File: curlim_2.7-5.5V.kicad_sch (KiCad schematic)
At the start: 9 parts, among them J11 Conn_01x02, J12 Conn_01x04, U4 AP22653AW6-7, U5 INA199A1DCKR

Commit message: WIP v0.2.0 changes
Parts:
- added R81: 10k, Resistor_SMD:R_0603_1608Metric_Pad0.98x0.95mm_HandSolder, symbol Device:R_Small
- RV1: LCSC (none) -> C118942; THT_LCSC C118942 -> (none)
- renumbered J11 to J10, J12 to J11
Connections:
- net EN: now also R81.1
- net GND: now also J10.1 (Pin_1), R81.2; no longer J10.2 (Pin_2)
- net ILIM: now also J10.2 (Pin_2); no longer J10.1 (Pin_1)

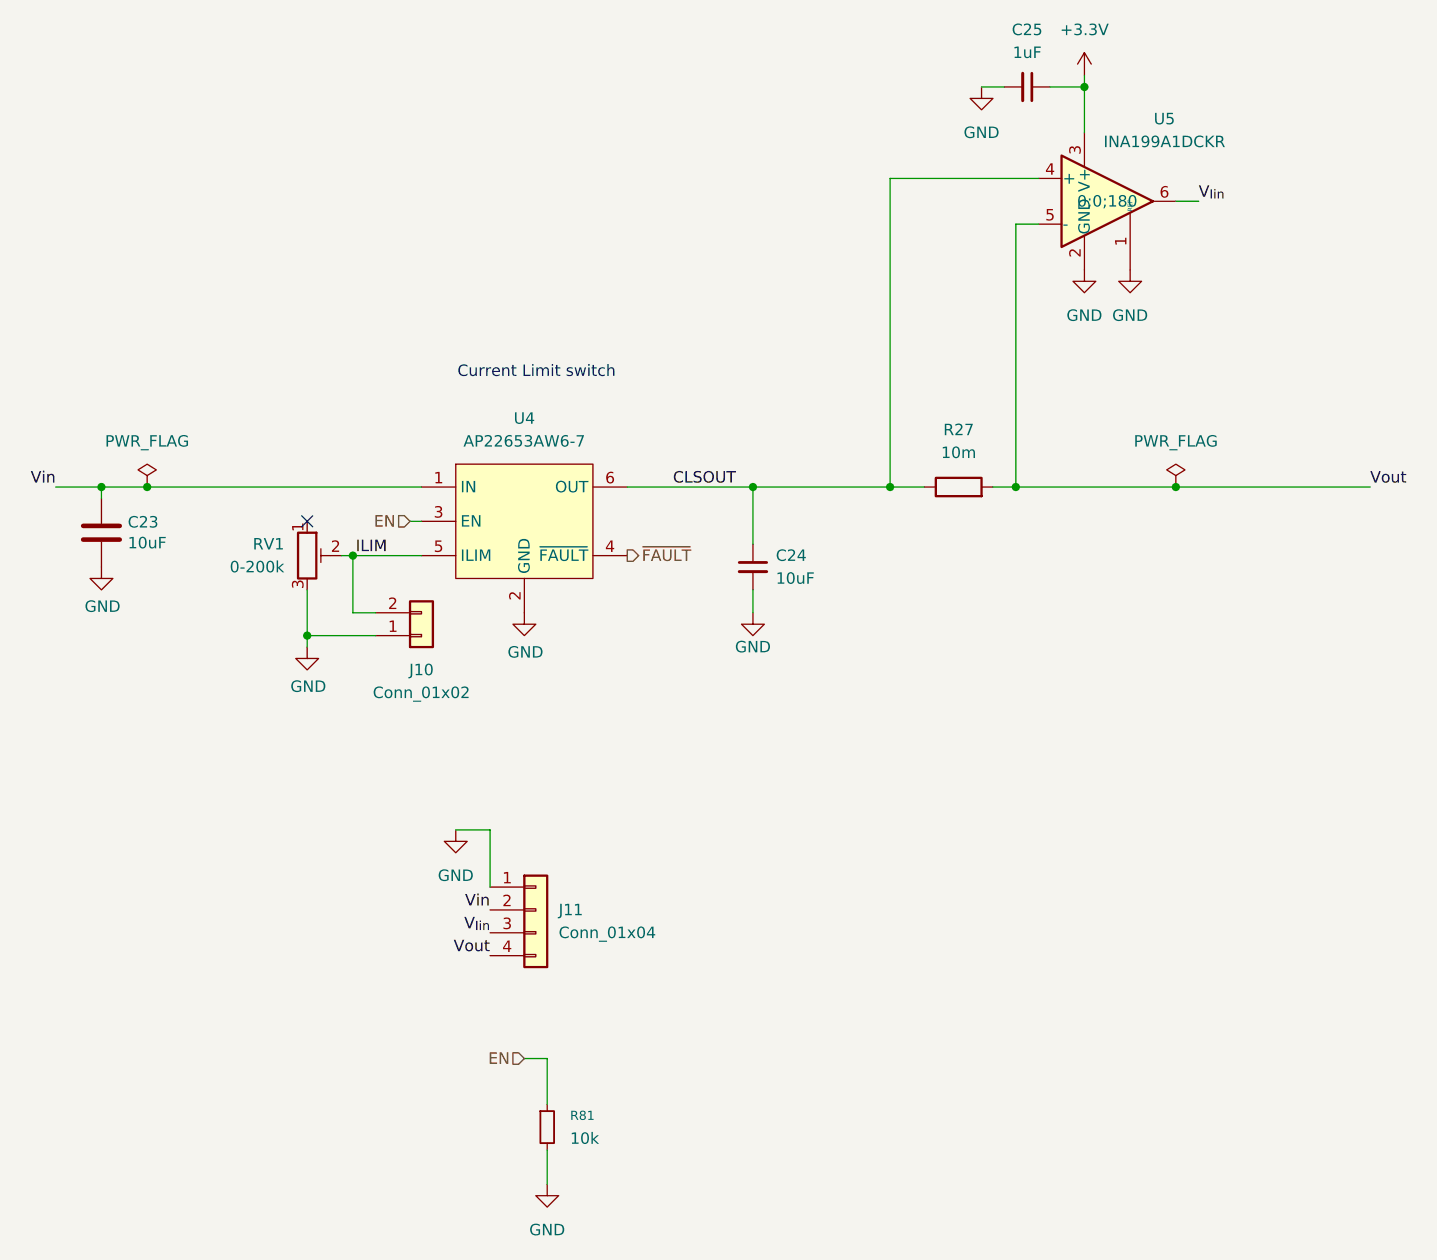
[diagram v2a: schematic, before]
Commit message: Assign part numbers and finish other 0.2.0 changes
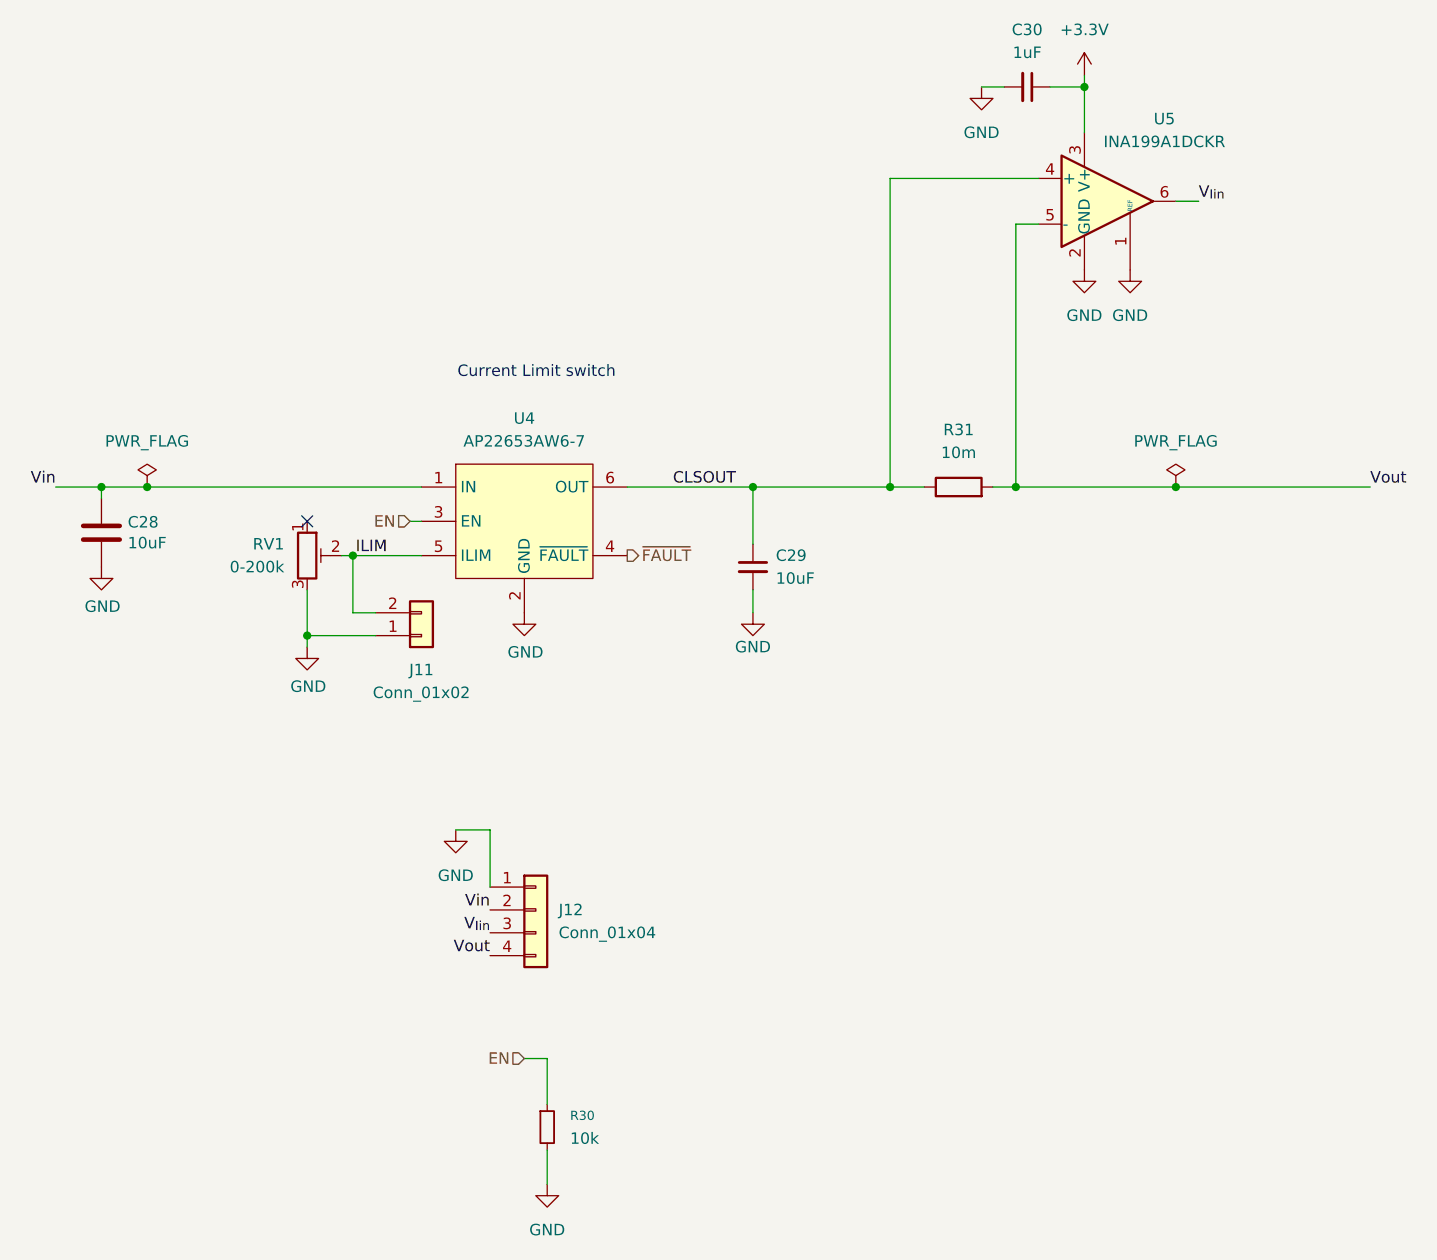
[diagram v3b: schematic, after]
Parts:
- J12: renamed from J11; LCSC (none) -> C2691448
- renumbered C23 to C28, C24 to C29, C25 to C30, J10 to J11, R81 to R30, R27 to R31

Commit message: Update the title blocks
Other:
- company: (none) -> Hat Labs Oy
- title: (none) -> HALSPA - Hat Labs Spaghetti Board
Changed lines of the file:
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@@
 	(generator_version "9.0")
 	(paper "A4")
+	(title_block
+		(title "HALSPA - Hat Labs Spaghetti Board")
+		(date "2025-04-17")
+		(rev "v0.2.0")
+		(company "Hat Labs Oy")
+		(comment 1 "See the accompanying LICENSE.md file for license details.")
+	)
 	(text "Current Limit switch"
 		(exclude_from_sim no)

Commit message: Add JLCPCB corrections
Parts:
- J12: JLCPCB_CORRECTION (none) -> 0;3.81;270
- RV1: JLCPCB_CORRECTION (none) -> 0;0;90; now in the parts list
- U4: JLCPCB_CORRECTION 0;0;90 -> 0;0;270
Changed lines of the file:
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@@
 			)
 		)
-		(property "JLCPCB_CORRECTION" "0;0;90"
+		(property "JLCPCB_CORRECTION" "0;0;270"
 			(at 134.62 82.55 0)
 			(effects
@@
 			)
 		)
+		(property "JLCPCB_CORRECTION" "0;3.81;270"
+			(at 135.89 125.73 0)
+			(effects
+				(font
+					(size 1.27 1.27)
+				)
+				(hide yes)
+			)
+		)
 		(pin "2"
 		)
@@
 		(unit 1)
 		(exclude_from_sim no)
-		(in_bom no)
+		(in_bom yes)
 		(on_board yes)
 		(dnp no)
@@
 			(at 110.49 86.36 0)
 			(effects
+				(font
+					(size 1.27 1.27)
+				)
+				(hide yes)
+			)
+		)
+		(property "JLCPCB_CORRECTION" "0;0;90"
+			(at 110.49 86.36 0)
+			(effects
